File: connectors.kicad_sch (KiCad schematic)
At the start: 29 parts, among them J10 Conn_01x06, J11 Conn_01x04, J12 USB4085-GF-A, J13 Conn_01x02, J6 FTSH-107-01-L-DV-K-TR, J7 Conn_01x02, J8 Conn_01x02, J9 Conn_01x07

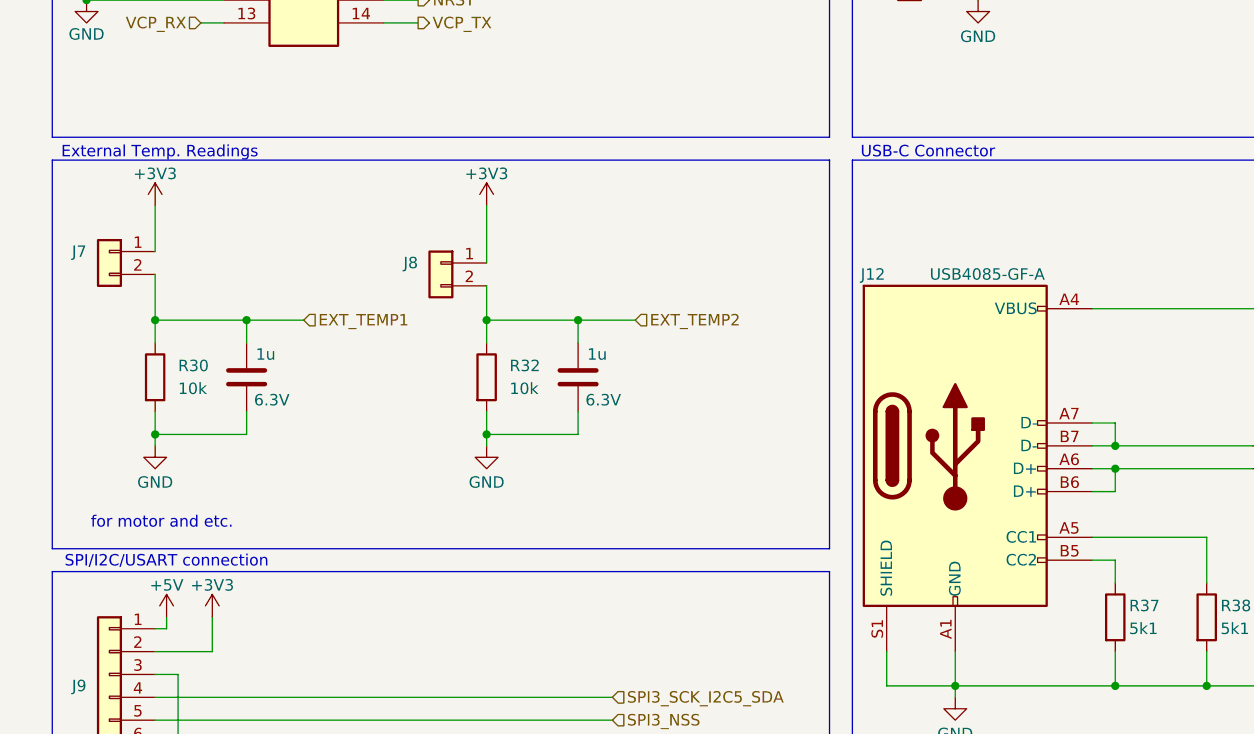
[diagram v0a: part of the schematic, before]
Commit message: Analog current filters were removed, some footprints were fixed and initial rough layout has been made.
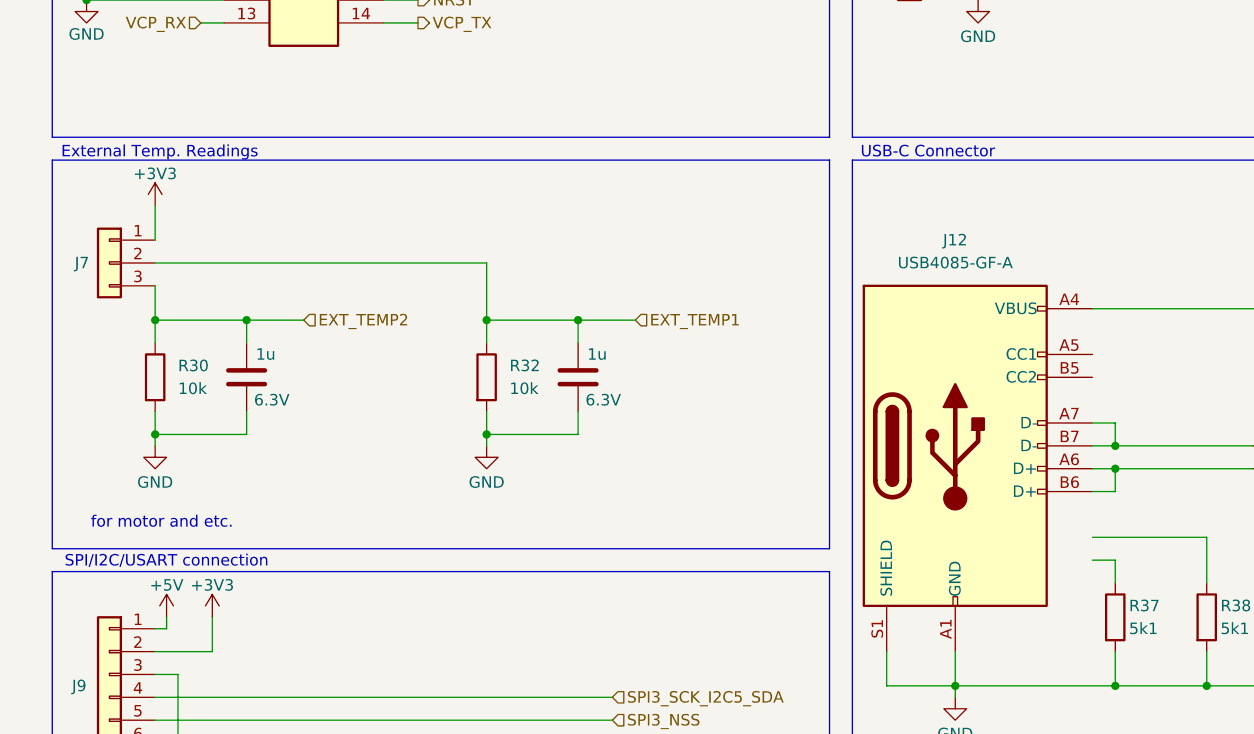
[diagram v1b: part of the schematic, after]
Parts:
- removed J12: USB4085-GF-A, Connector_USB:USB_C_Receptacle_GCT_USB4085, symbol Connector:USB_C_Receptacle_USB2.0_14P
- removed J7, J8: Conn_01x02, Connector_JST:JST_XH_B2B-XH-A_1x02_P2.50mm_Vertical, symbol Connector_Generic:Conn_01x02
- added J12: USB4085-GF-A, Connector_USB:USB_C_Receptacle_GCT_USB4085, symbol NanoGaN:USB_C_Receptacle_USB2.0_14P
- added J7: Conn_01x03, Connector_JST:JST_EH_B3B-EH-A_1x03_P2.50mm_Vertical, symbol Connector_Generic:Conn_01x03
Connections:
- net +3V3: now also J7.1 (Pin_1)
- net EXT_TEMP1: now also C53.1, R32.1, J7.2 (Pin_2); no longer C52.1, R30.1
- net EXT_TEMP2: now also C52.1, R30.1, J7.3 (Pin_3); no longer C53.1, R32.1
- net GND: now also J12.A1 (GND), J12.A12 (GND), J12.B1 (GND), J12.B12 (GND), J12.S1 (SHIELD)
- net at C67.1, D2.5 (VBUS), J13.1 (Pin_1)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: now also J12.A4 (VBUS), J12.A9 (VBUS), J12.B4 (VBUS), J12.B9 (VBUS)
- net at D2.4 (I/O2): now also J12.A6 (D+), J12.B6 (D+)
- net at D2.6 (I/O1): now also J12.A7 (D-), J12.B7 (D-)

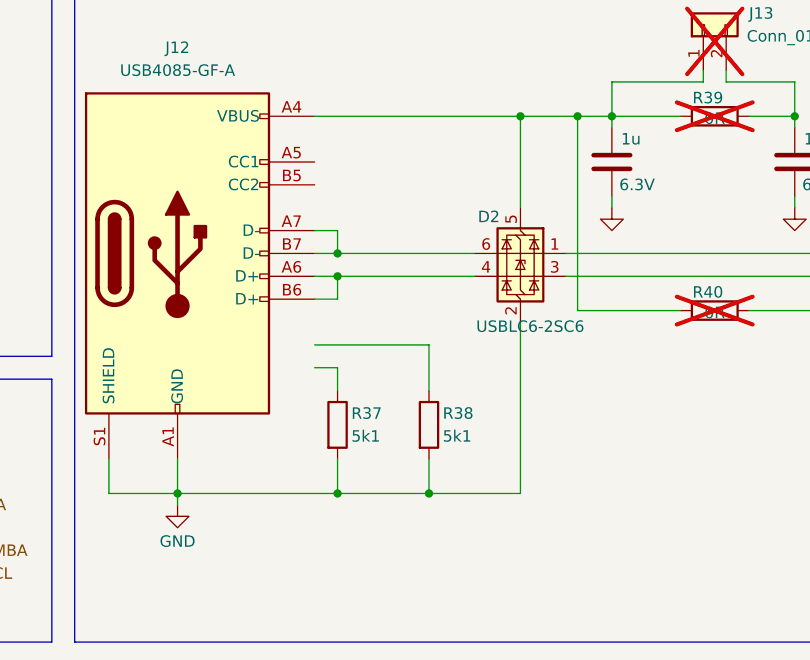
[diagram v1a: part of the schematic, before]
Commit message: Updated the DC/DC converter from I_out = 2A to 3.5A  and fsw = 1.1MHz to 400kHz
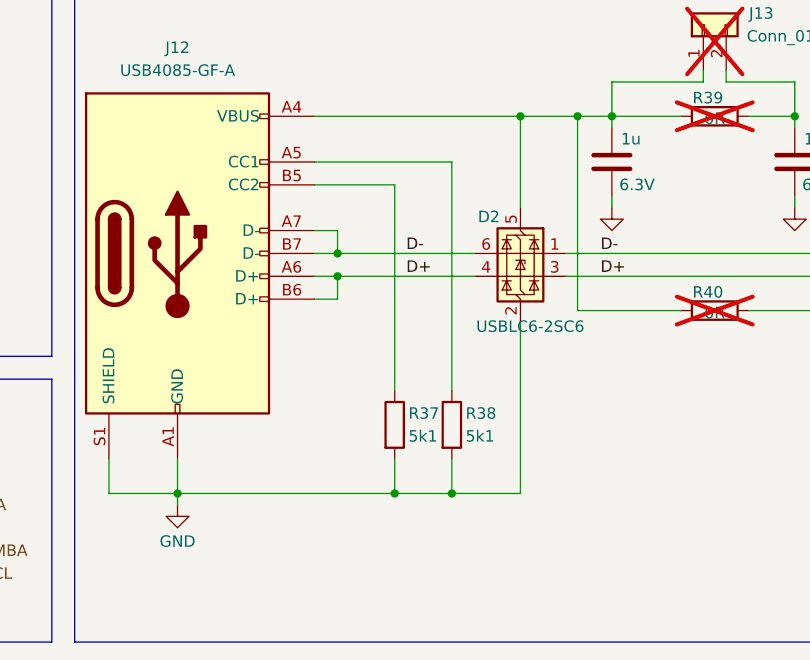
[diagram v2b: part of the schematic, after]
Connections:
- net D+: now also D2.4 (I/O2), J12.A6 (D+), J12.B6 (D+)
- net D-: now also D2.6 (I/O1), J12.A7 (D-), J12.B7 (D-)
- net at R38.1: now also J12.A5 (CC1)
- net at J12.B5 (CC2): now also R37.1
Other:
- moved on the sheet: R37, R38
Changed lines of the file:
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@@
 	)
 	(junction
-		(at 143.51 111.76)
+		(at 38.1 149.86)
 		(diameter 0)
 		(color 0 0 0 0)
 	)
 	(junction
-		(at 38.1 149.86)
+		(at 26.67 71.12)
 		(diameter 0)
 		(color 0 0 0 0)
 	)
 	(junction
-		(at 26.67 71.12)
+		(at 63.5 83.82)
 		(diameter 0)
 		(color 0 0 0 0)
 	)
 	(junction
-		(at 133.35 111.76)
+		(at 36.83 71.12)
 		(diameter 0)
 		(color 0 0 0 0)
 	)
 	(junction
-		(at 63.5 83.82)
+		(at 26.67 83.82)
 		(diameter 0)
 		(color 0 0 0 0)
 	)
 	(junction
-		(at 36.83 71.12)
+		(at 139.7 111.76)
 		(diameter 0)
 		(color 0 0 0 0)
 	)
 	(junction
-		(at 26.67 83.82)
+		(at 146.05 111.76)
 		(diameter 0)
 		(color 0 0 0 0)
@@
 	(wire
 		(pts
-			(xy 143.51 95.25) (xy 143.51 100.33)
+			(xy 146.05 74.93) (xy 146.05 100.33)
 		)
 		(stroke
@@
 	(wire
 		(pts
-			(xy 133.35 111.76) (xy 143.51 111.76)
-		)
-		(stroke
-			(width 0)
-			(type default)
-		)
-	)
-	(wire
-		(pts
-			(xy 143.51 107.95) (xy 143.51 111.76)
+			(xy 146.05 107.95) (xy 146.05 111.76)
 		)
 		(stroke
@@
 	(wire
 		(pts
-			(xy 143.51 111.76) (xy 153.67 111.76)
-		)
-		(stroke
-			(width 0)
-			(type default)
-		)
-	)
-	(wire
-		(pts
 			(xy 26.67 67.31) (xy 26.67 71.12)
 		)
@@
 	(wire
 		(pts
+			(xy 139.7 111.76) (xy 146.05 111.76)
+		)
+		(stroke
+			(width 0)
+			(type default)
+		)
+	)
+	(wire
+		(pts
 			(xy 55.88 144.78) (xy 55.88 154.94)
 		)
@@
 	(wire
 		(pts
-			(xy 27.94 144.78) (xy 29.21 144.78)
+			(xy 146.05 74.93) (xy 130.81 74.93)
 		)
 		(stroke
@@
 	(wire
 		(pts
-			(xy 115.57 34.29) (xy 118.11 34.29)
+			(xy 27.94 144.78) (xy 29.21 144.78)
 		)
 		(stroke
@@
 	(wire
 		(pts
-			(xy 29.21 157.48) (xy 27.94 157.48)
+			(xy 115.57 34.29) (xy 118.11 34.29)
 		)
 		(stroke
@@
 	(wire
 		(pts
-			(xy 46.99 144.78) (xy 46.99 152.4)
+			(xy 29.21 157.48) (xy 27.94 157.48)
 		)
 		(stroke
@@
 	(wire
 		(pts
-			(xy 26.67 115.57) (xy 77.47 115.57)
+			(xy 46.99 144.78) (xy 46.99 152.4)
 		)
 		(stroke
@@
 	(wire
 		(pts
-			(xy 179.07 69.85) (xy 184.15 69.85)
+			(xy 26.67 115.57) (xy 77.47 115.57)
 		)
 		(stroke
@@
 	(wire
 		(pts
-			(xy 130.81 85.09) (xy 133.35 85.09)
+			(xy 179.07 69.85) (xy 184.15 69.85)
 		)
 		(stroke
@@
 	(wire
 		(pts
-			(xy 26.67 113.03) (xy 77.47 113.03)
+			(xy 130.81 85.09) (xy 133.35 85.09)
 		)
 		(stroke
@@
 	(wire
 		(pts
-			(xy 130.81 95.25) (xy 143.51 95.25)
+			(xy 26.67 113.03) (xy 77.47 113.03)
 		)
 		(stroke
@@
 	(wire
 		(pts
-			(xy 115.57 111.76) (xy 133.35 111.76)
+			(xy 115.57 111.76) (xy 139.7 111.76)
 		)
 		(stroke
@@
 	(wire
 		(pts
+			(xy 130.81 77.47) (xy 139.7 77.47)
+		)
+		(stroke
+			(width 0)
+			(type default)
+		)
+	)
+	(wire
+		(pts
 			(xy 55.88 135.89) (xy 55.88 137.16)
 		)
@@
 	(wire
 		(pts
+			(xy 146.05 111.76) (xy 153.67 111.76)
+		)
+		(stroke
+			(width 0)
+			(type default)
+		)
+	)
+	(wire
+		(pts
 			(xy 115.57 31.75) (xy 194.31 31.75)
 		)
@@
 	(wire
 		(pts
-			(xy 133.35 107.95) (xy 133.35 111.76)
+			(xy 139.7 107.95) (xy 139.7 111.76)
 		)
 		(stroke
@@
 	(wire
 		(pts
-			(xy 133.35 97.79) (xy 133.35 100.33)
+			(xy 139.7 77.47) (xy 139.7 100.33)
 		)
 		(stroke
@@
 	(wire
 		(pts
-			(xy 130.81 97.79) (xy 133.35 97.79)
-		)
-		(stroke
-			(width 0)
-			(type default)
-		)
-	)
-	(wire
-		(pts
 			(xy 184.15 66.04) (xy 184.15 69.85)
 		)
@@
 		)
 	)
+	(label "D-"
+		(at 162.56 85.09 0)
+		(effects
+			(font
+				(size 1.27 1.27)
+			)
+			(justify left bottom)
+		)
+	)
+	(label "D-"
+		(at 140.97 85.09 0)
+		(effects
+			(font
+				(size 1.27 1.27)
+			)
+			(justify left bottom)
+		)
+	)
+	(label "D+"
+		(at 162.56 87.63 0)
+		(effects
+			(font
+				(size 1.27 1.27)
+			)
+			(justify left bottom)
+		)
+	)
+	(label "D+"
+		(at 140.97 87.63 0)
+		(effects
+			(font
+				(size 1.27 1.27)
+			)
+			(justify left bottom)
+		)
+	)
 	(hierarchical_label "D+"
 		(shape bidirectional)
@@
 	(symbol
 		(lib_id "Device:R")
-		(at 143.51 104.14 0)
+		(at 146.05 104.14 0)
 		(unit 1)
 		(exclude_from_sim no)
@@
 		(dnp no)
 		(property "Reference" "R38"
-			(at 145.034 102.87 0)
+			(at 147.574 102.87 0)
 			(effects
 				(font
@@
 		)
 		(property "Value" "5k1"
-			(at 145.034 105.41 0)
+			(at 147.574 105.41 0)
 			(effects
 				(font
@@
 		)
 		(property "Footprint" "Resistor_SMD:R_0402_1005Metric"
-			(at 141.732 104.14 90)
+			(at 144.272 104.14 90)
 			(effects
 				(font
@@
 		)
 		(property "Datasheet" "~"
-			(at 143.51 104.14 0)
+			(at 146.05 104.14 0)
 			(effects
 				(font
@@
 		)
 		(property "Description" "-55℃~+155℃ 5.1kΩ 50V 62.5mW Thick Film Resistor ±1% ±100ppm/℃ 0402 Chip Resistor - Surface Mount ROHS"
-			(at 143.51 104.14 0)
+			(at 146.05 104.14 0)
 			(effects
 				(font
@@
 		)
 		(property "LCSC" "C25905"
-			(at 143.51 104.14 0)
+			(at 146.05 104.14 0)
 			(effects
 				(font
@@
 	(symbol
 		(lib_id "Device:R")
-		(at 133.35 104.14 0)
+		(at 139.7 104.14 0)
 		(unit 1)
 		(exclude_from_sim no)
@@
 		(dnp no)
 		(property "Reference" "R37"
-			(at 134.874 102.87 0)
+			(at 141.224 102.87 0)
 			(effects
 				(font
@@
 		)
 		(property "Value" "5k1"
-			(at 134.874 105.41 0)
+			(at 141.224 105.41 0)
 			(effects
 				(font
@@
 		)
 		(property "Footprint" "Resistor_SMD:R_0402_1005Metric"
-			(at 131.572 104.14 90)
+			(at 137.922 104.14 90)
 			(effects
 				(font
@@
 		)
 		(property "Datasheet" "~"
-			(at 133.35 104.14 0)
+			(at 139.7 104.14 0)
 			(effects
 				(font
@@
 		)
 		(property "Description" "-55℃~+155℃ 5.1kΩ 50V 62.5mW Thick Film Resistor ±1% ±100ppm/℃ 0402 Chip Resistor - Surface Mount ROHS"
-			(at 133.35 104.14 0)
+			(at 139.7 104.14 0)
 			(effects
 				(font
@@
 		)
 		(property "LCSC" "C25905"
-			(at 133.35 104.14 0)
+			(at 139.7 104.14 0)
 			(effects
 				(font

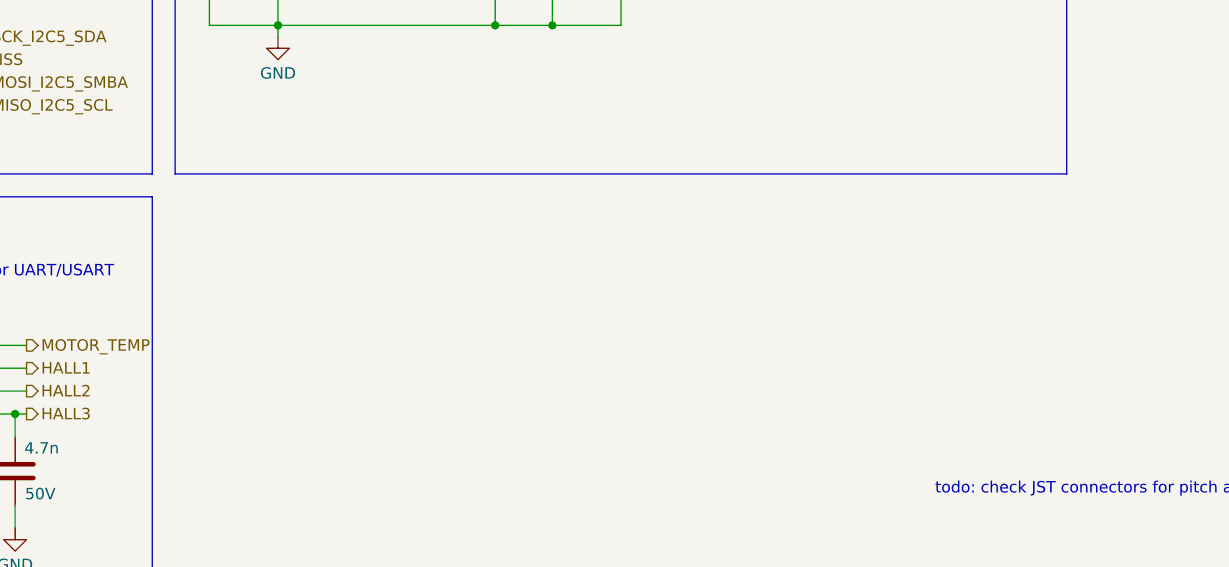
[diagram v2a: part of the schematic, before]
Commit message: added fan connector
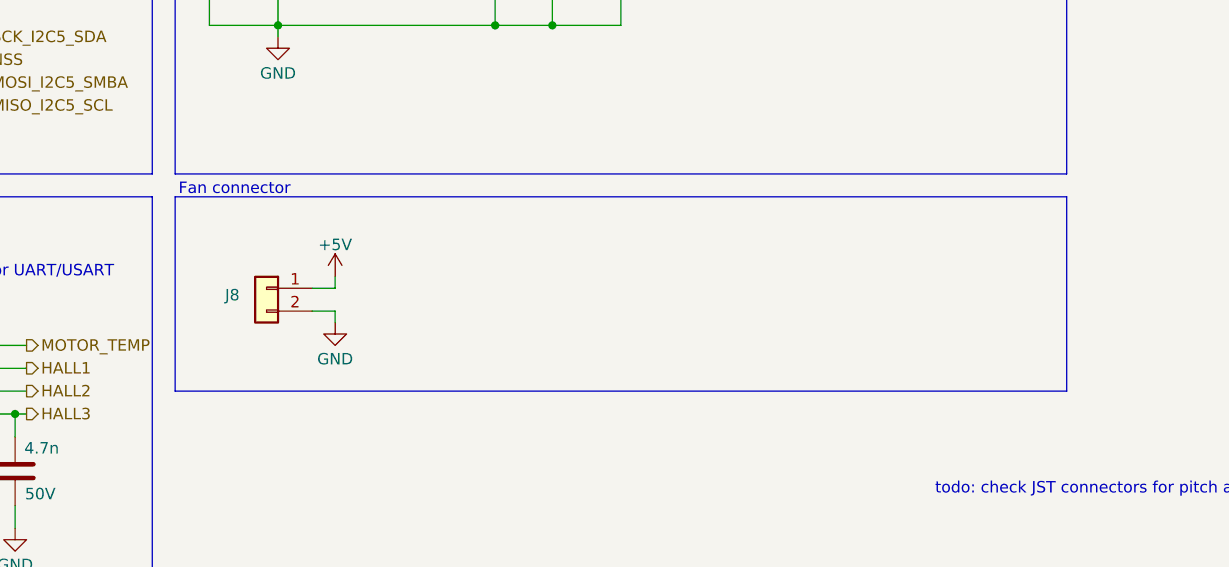
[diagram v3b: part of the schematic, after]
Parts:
- added J8: Conn_01x02, Connector_JST:JST_EH_B2B-EH-A_1x02_P2.50mm_Vertical, symbol Connector_Generic:Conn_01x02
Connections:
- net +5V: now also J8.1 (Pin_1)
- net GND: now also J8.2 (Pin_2)
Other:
- note added: "Fan connector"

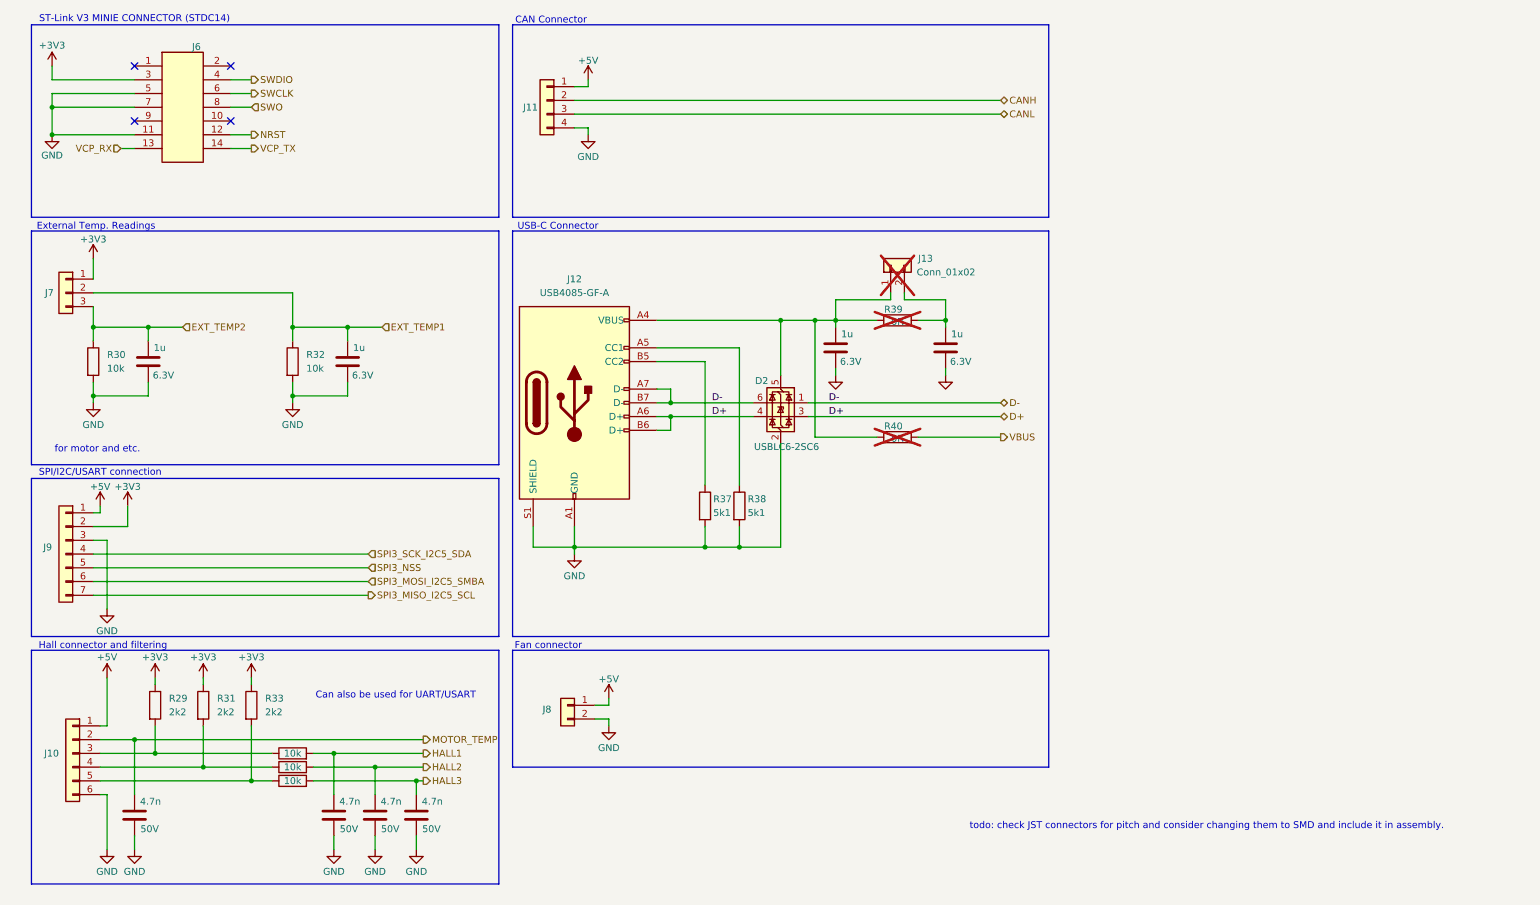
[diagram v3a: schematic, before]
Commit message: Added PWM fan control
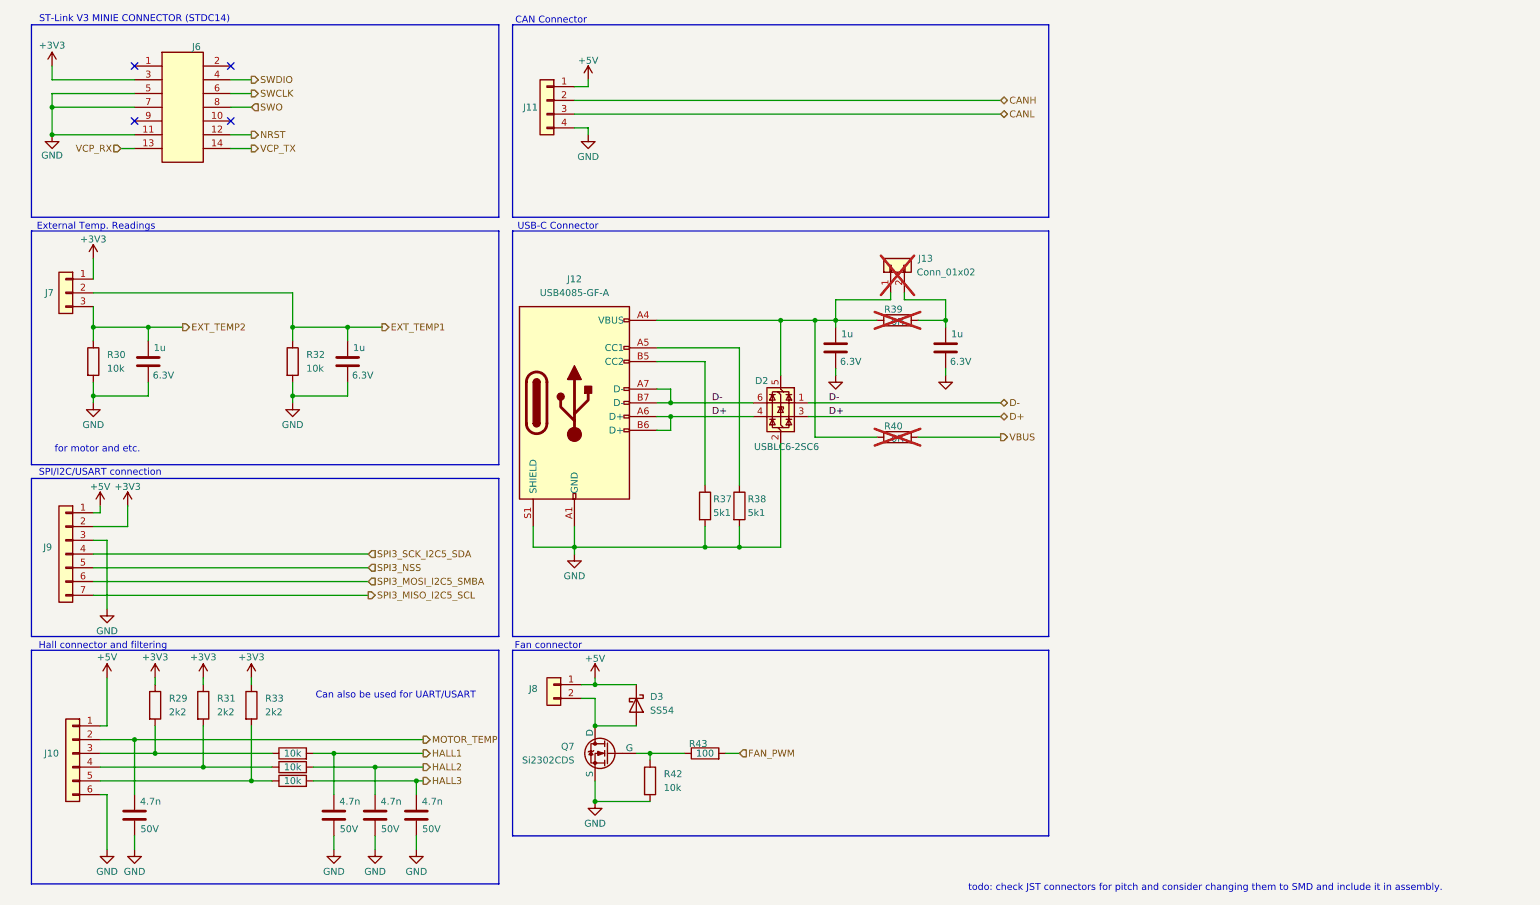
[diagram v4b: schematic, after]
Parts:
- added D3: SS54, Diode_SMD:D_SMA, symbol Device:D_Schottky
- added Q7: Si2302CDS, NanoGaN:SOT-23_Si2302CDS, symbol Simulation_SPICE:NMOS
- added R42: 10k, Resistor_SMD:R_0603_1608Metric, symbol Device:R
- added R43: 100, Resistor_SMD:R_0402_1005Metric, symbol Device:R
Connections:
- net +5V: now also D3.1 (K)
- net GND: now also Q7.3 (S), R42.2; no longer J8.2 (Pin_2)
- new net: D3.2 (A), J8.2 (Pin_2), Q7.1 (D)
- new net: Q7.2 (G), R42.1, R43.1
- new net FAN_PWM: R43.2
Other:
- moved on the sheet: J8
